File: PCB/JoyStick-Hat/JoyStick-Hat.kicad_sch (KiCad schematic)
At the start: 0 parts

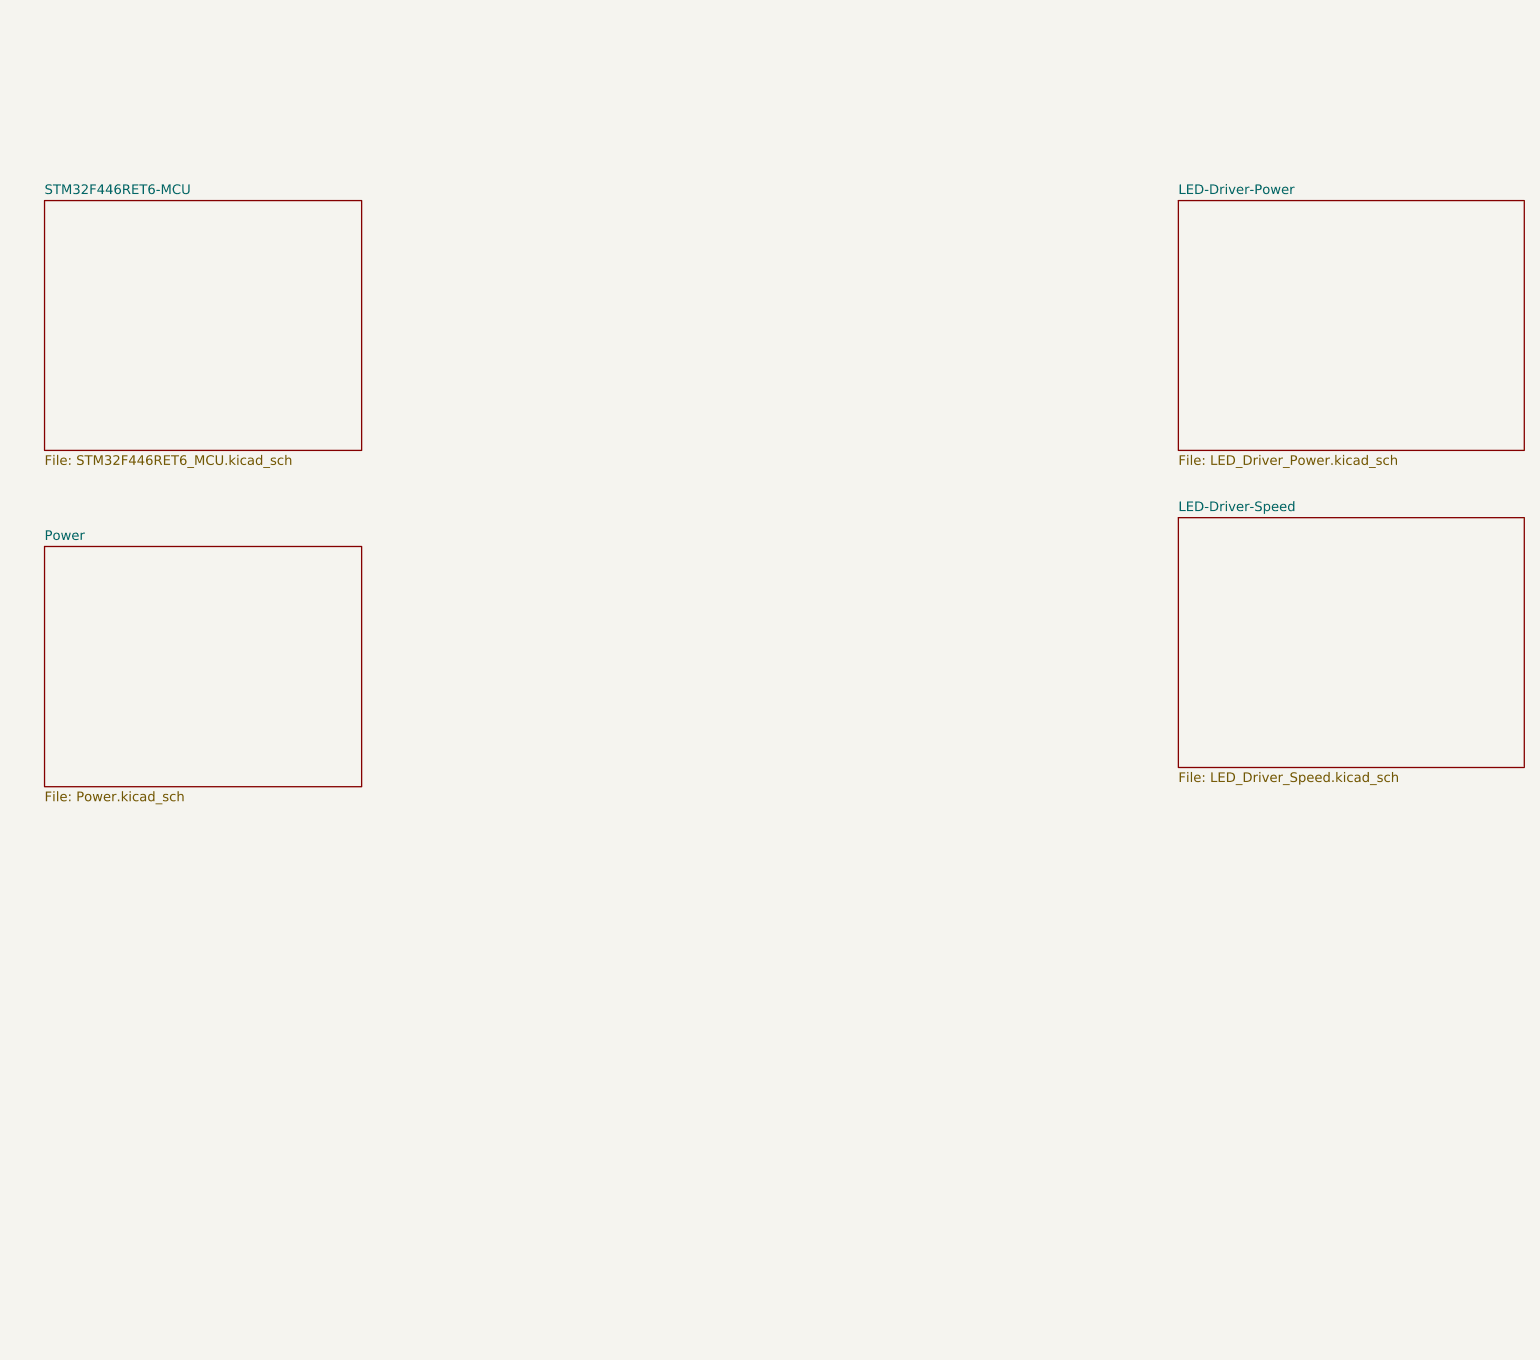
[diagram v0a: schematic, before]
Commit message: Power and LED Driver
Power Supply Schematic sketched out using Pololu power regulator modules to hasten design. LED drivers replaced with ones that have 24 ouputs so we can use 20 unit bar graph LEDs and have 8 extra channels for other onboard LEDs
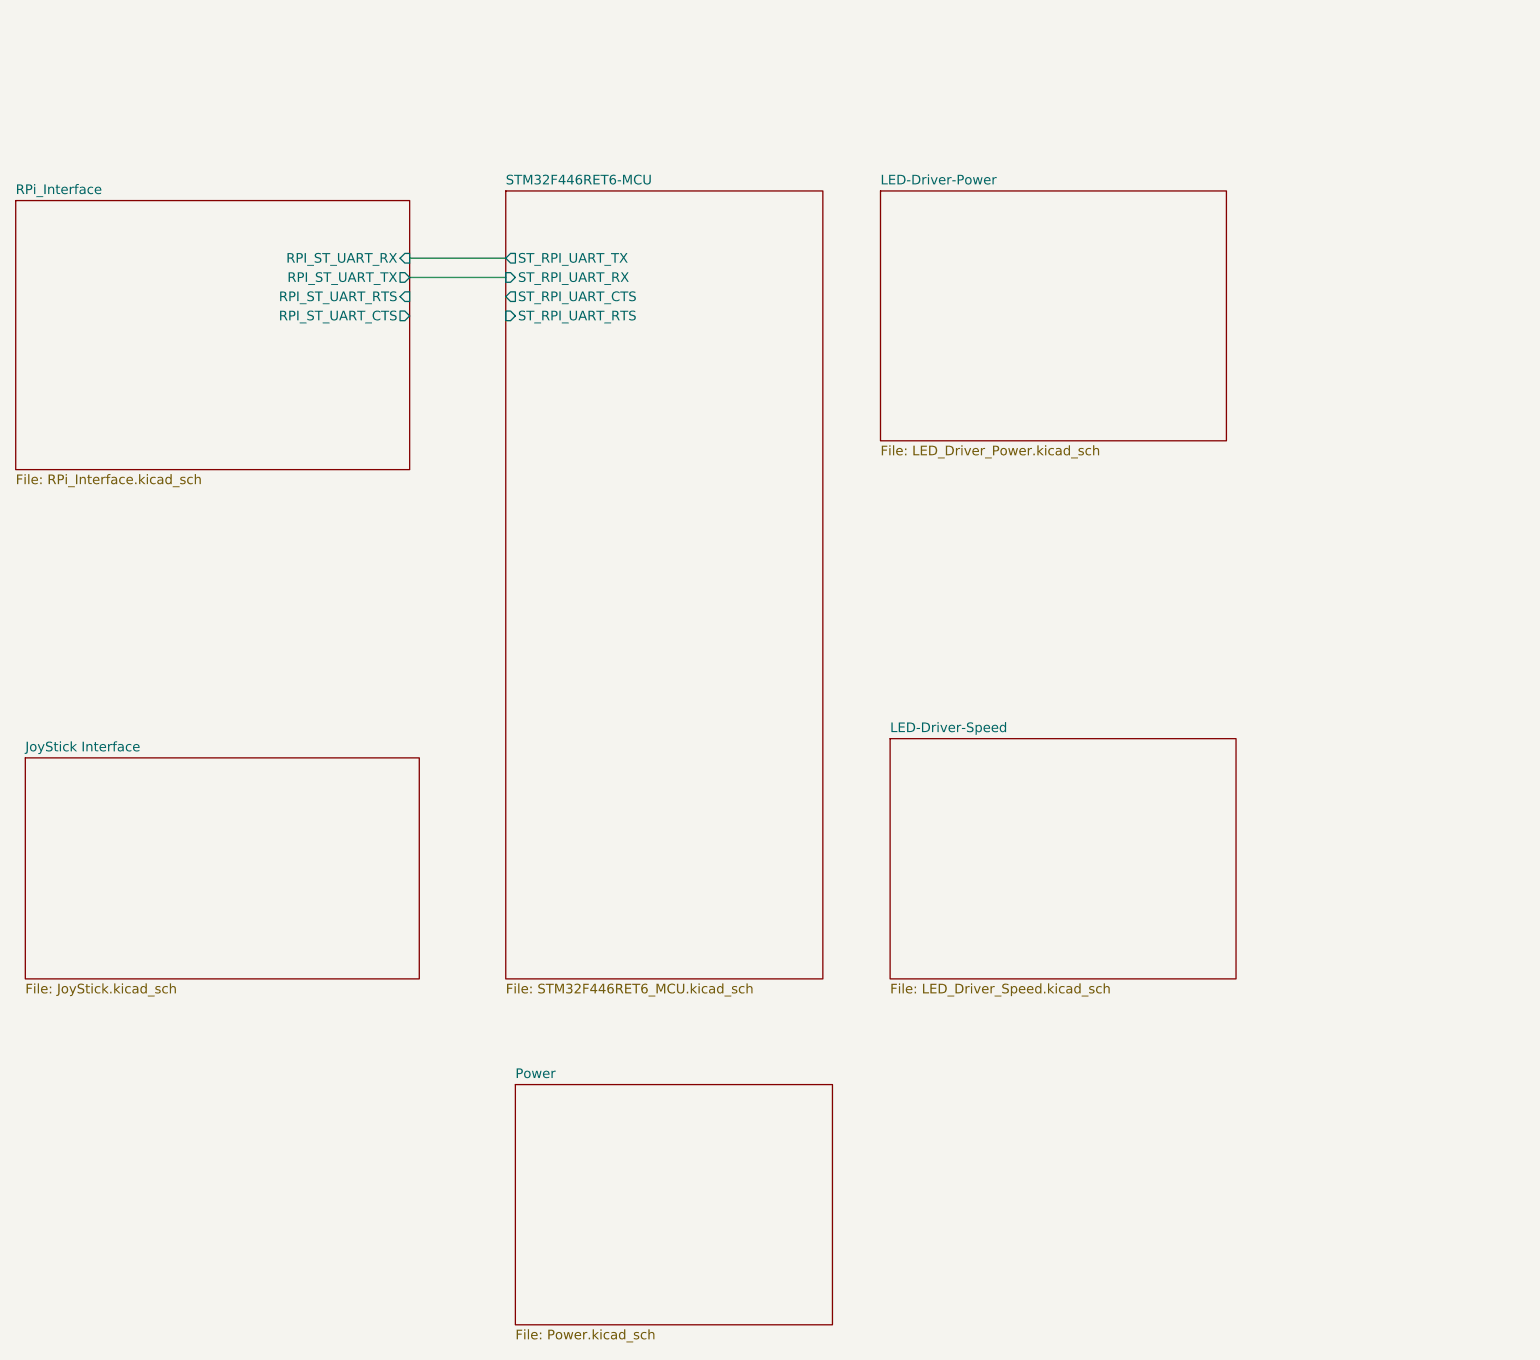
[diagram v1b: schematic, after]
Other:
- added sheet JoyStick Interface (JoyStick.kicad_sch)
- added sheet RPi_Interface (RPi_Interface.kicad_sch)
- sheet STM32F446RET6-MCU ports: added ST_RPI_UART_CTS, ST_RPI_UART_RTS, ST_RPI_UART_RX, ST_RPI_UART_TX; removed none
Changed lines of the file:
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@@
 (kicad_sch (version 20230121) (generator eeschema)
   (paper "A4")
-  (sheet (at 201.93 85.09) (size 45.72 33.02) (fields_autoplaced)
+  (wire (pts (xy 100.33 53.34) (xy 113.03 53.34))
+    (stroke (width 0) (type default))
+  )
+  (wire (pts (xy 100.33 50.8) (xy 113.03 50.8))
+    (stroke (width 0) (type default))
+  )
+  (sheet (at 163.83 114.3) (size 45.72 31.75) (fields_autoplaced)
     (stroke (width 0.1524) (type solid))
     (fill (color 255 255 0 1.0000))
-    (property "Sheetname" "LED-Driver-Speed" (at 201.93 84.3784 0)
+    (property "Sheetname" "LED-Driver-Speed" (at 163.83 113.5884 0)
       (effects (font (size 1.27 1.27)) (justify left bottom))
     )
-    (property "Sheetfile" "LED_Driver_Speed.kicad_sch" (at 201.93 118.6946 0)
+    (property "Sheetfile" "LED_Driver_Speed.kicad_sch" (at 163.83 146.6346 0)
       (effects (font (size 1.27 1.27)) (justify left top))
     )
@@
     )
   )
-  (sheet (at 201.93 43.18) (size 45.72 33.02) (fields_autoplaced)
+  (sheet (at 49.53 116.84) (size 52.07 29.21) (fields_autoplaced)
+    (stroke (width 0.1524) (type solid))
+    (fill (color 255 0 255 1.0000))
+    (property "Sheetname" "JoyStick Interface" (at 49.53 116.1284 0)
+      (effects (font (size 1.27 1.27)) (justify left bottom))
+    )
+    (property "Sheetfile" "JoyStick.kicad_sch" (at 49.53 146.6346 0)
+      (effects (font (size 1.27 1.27)) (justify left top))
+    )
+    (instances
+      (project "JoyStick-Hat"
+        (path "/cf0c81b5-5bdf-47c3-83c0-f6980f515e65" (page "7"))
+      )
+    )
+  )
+  (sheet (at 48.26 43.18) (size 52.07 35.56) (fields_autoplaced)
+    (stroke (width 0.1524) (type solid))
+    (fill (color 0 194 0 1.0000))
+    (property "Sheetname" "RPi_Interface" (at 48.26 42.4684 0)
+      (effects (font (size 1.27 1.27)) (justify left bottom))
+    )
+    (property "Sheetfile" "RPi_Interface.kicad_sch" (at 48.26 79.3246 0)
+      (effects (font (size 1.27 1.27)) (justify left top))
+    )
+    (pin "RPI_ST_UART_RX" input (at 100.33 50.8 0)
+      (effects (font (size 1.27 1.27)) (justify right))
+    )
+    (pin "RPI_ST_UART_TX" output (at 100.33 53.34 0)
+      (effects (font (size 1.27 1.27)) (justify right))
+    )
+    (pin "RPI_ST_UART_RTS" input (at 100.33 55.88 0)
+      (effects (font (size 1.27 1.27)) (justify right))
+    )
+    (pin "RPI_ST_UART_CTS" output (at 100.33 58.42 0)
+      (effects (font (size 1.27 1.27)) (justify right))
+    )
+    (instances
+      (project "JoyStick-Hat"
+        (path "/cf0c81b5-5bdf-47c3-83c0-f6980f515e65" (page "6"))
+      )
+    )
+  )
+  (sheet (at 162.56 41.91) (size 45.72 33.02) (fields_autoplaced)
     (stroke (width 0.1524) (type solid))
     (fill (color 255 255 0 1.0000))
-    (property "Sheetname" "LED-Driver-Power" (at 201.93 42.4684 0)
+    (property "Sheetname" "LED-Driver-Power" (at 162.56 41.1984 0)
       (effects (font (size 1.27 1.27)) (justify left bottom))
     )
-    (property "Sheetfile" "LED_Driver_Power.kicad_sch" (at 201.93 76.7846 0)
+    (property "Sheetfile" "LED_Driver_Power.kicad_sch" (at 162.56 75.5146 0)
       (effects (font (size 1.27 1.27)) (justify left top))
     )
@@
     )
   )
-  (sheet (at 52.07 88.9) (size 41.91 31.75) (fields_autoplaced)
+  (sheet (at 114.3 160.02) (size 41.91 31.75) (fields_autoplaced)
     (stroke (width 0.1524) (type solid))
     (fill (color 255 0 0 1.0000))
-    (property "Sheetname" "Power" (at 52.07 88.1884 0)
+    (property "Sheetname" "Power" (at 114.3 159.3084 0)
       (effects (font (size 1.27 1.27)) (justify left bottom))
     )
-    (property "Sheetfile" "Power.kicad_sch" (at 52.07 121.2346 0)
+    (property "Sheetfile" "Power.kicad_sch" (at 114.3 192.3546 0)
       (effects (font (size 1.27 1.27)) (justify left top))
     )
@@
     )
   )
-  (sheet (at 52.07 43.18) (size 41.91 33.02) (fields_autoplaced)
+  (sheet (at 113.03 41.91) (size 41.91 104.14) (fields_autoplaced)
     (stroke (width 0.1524) (type solid))
     (fill (color 0 255 255 1.0000))
-    (property "Sheetname" "STM32F446RET6-MCU" (at 52.07 42.4684 0)
+    (property "Sheetname" "STM32F446RET6-MCU" (at 113.03 41.1984 0)
       (effects (font (size 1.27 1.27)) (justify left bottom))
     )
-    (property "Sheetfile" "STM32F446RET6_MCU.kicad_sch" (at 52.07 76.7846 0)
+    (property "Sheetfile" "STM32F446RET6_MCU.kicad_sch" (at 113.03 146.6346 0)
       (effects (font (size 1.27 1.27)) (justify left top))
     )
+    (pin "ST_RPI_UART_CTS" output (at 113.03 55.88 180)
+      (effects (font (size 1.27 1.27)) (justify left))
+    )
+    (pin "ST_RPI_UART_RX" input (at 113.03 53.34 180)
+      (effects (font (size 1.27 1.27)) (justify left))
+    )
+    (pin "ST_RPI_UART_TX" output (at 113.03 50.8 180)
+      (effects (font (size 1.27 1.27)) (justify left))
+    )
+    (pin "ST_RPI_UART_RTS" input (at 113.03 58.42 180)
+      (effects (font (size 1.27 1.27)) (justify left))
+    )
     (instances
